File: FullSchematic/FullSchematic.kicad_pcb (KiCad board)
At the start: 4 copper layers, 106 parts, among them J1 USB_A, J10 LCD_Conn, J2 ATX-24, J3 Red Banana Jack, J4 Black Banana Jack, J5 2x6 Pin Header, J6 2x6 Pin Header, J7 CT3151-2, J8 CT3151-2, J9 2x6 Pin Header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

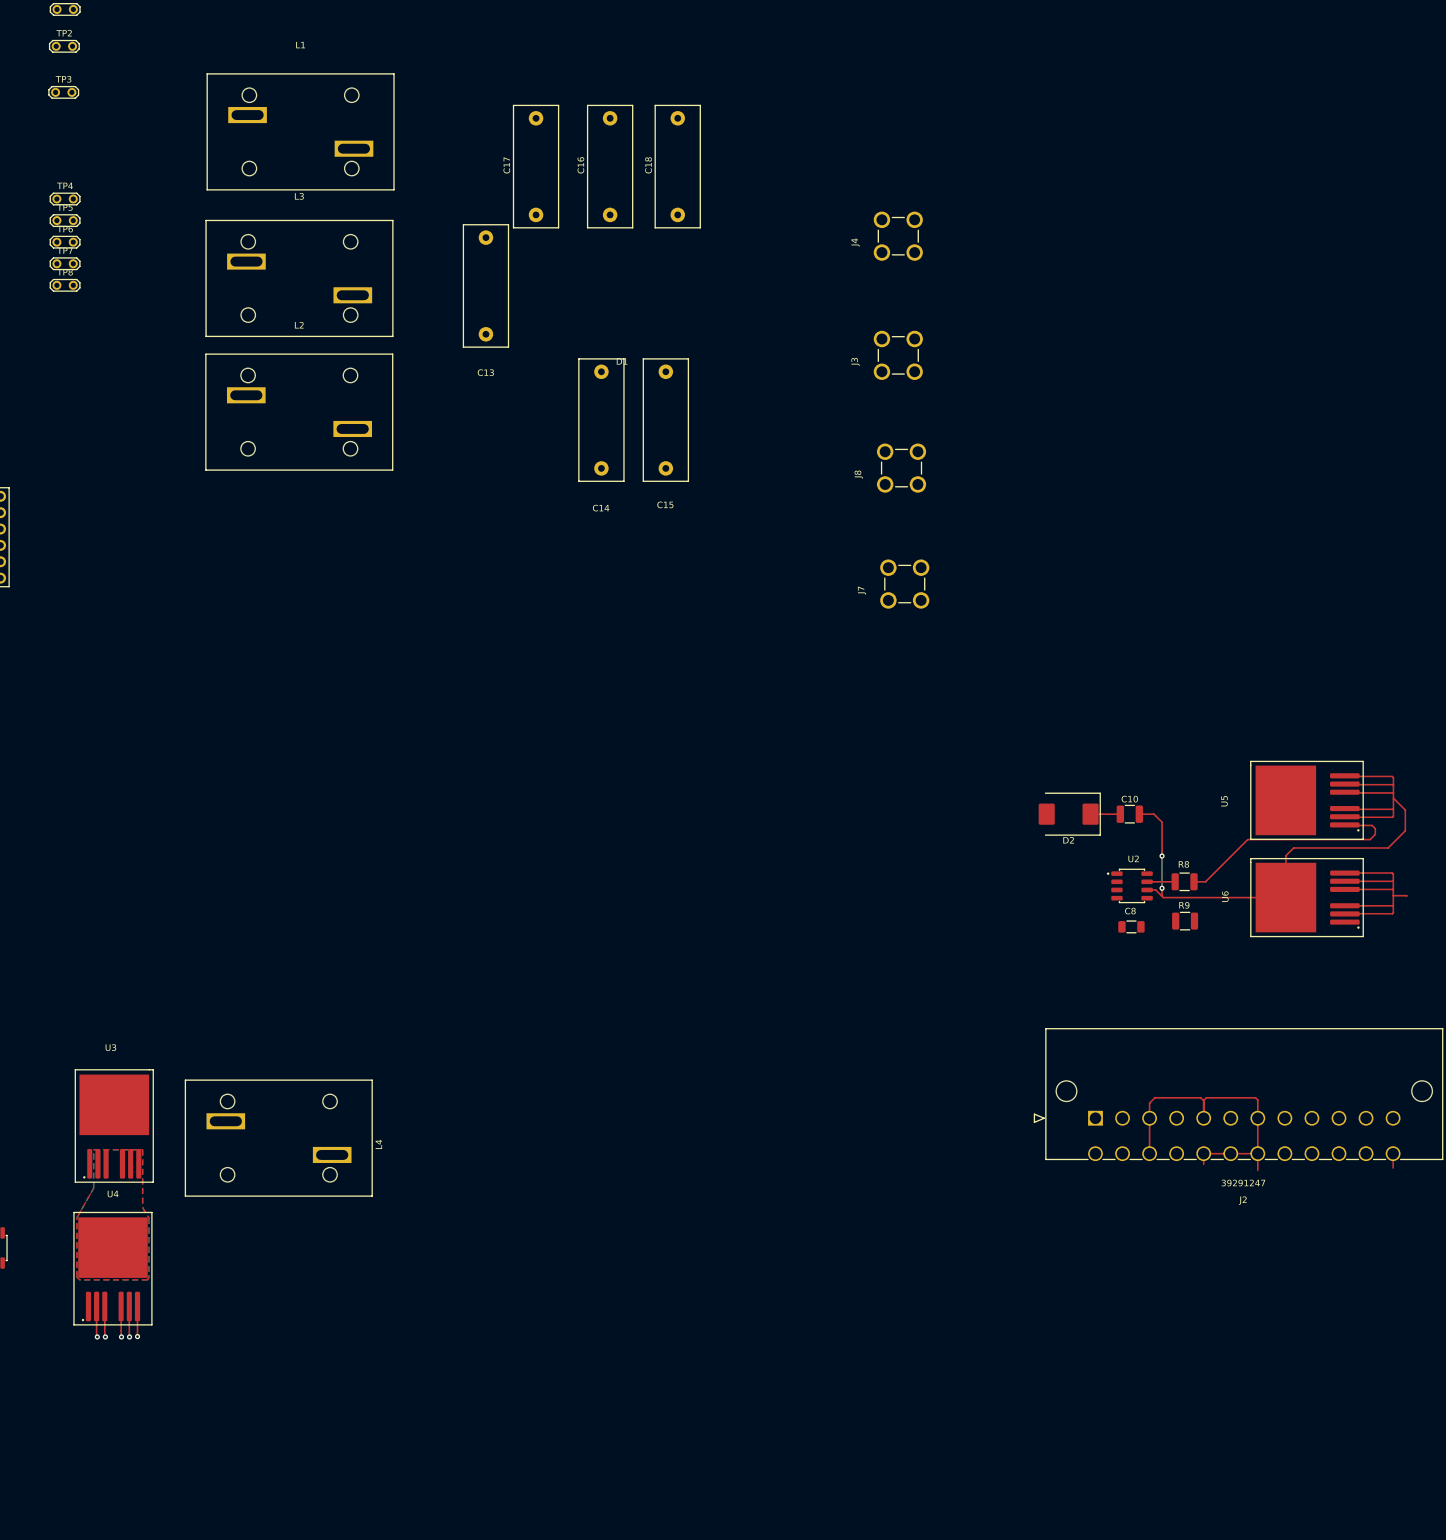
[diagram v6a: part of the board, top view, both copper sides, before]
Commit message: More Accurate Power Traces
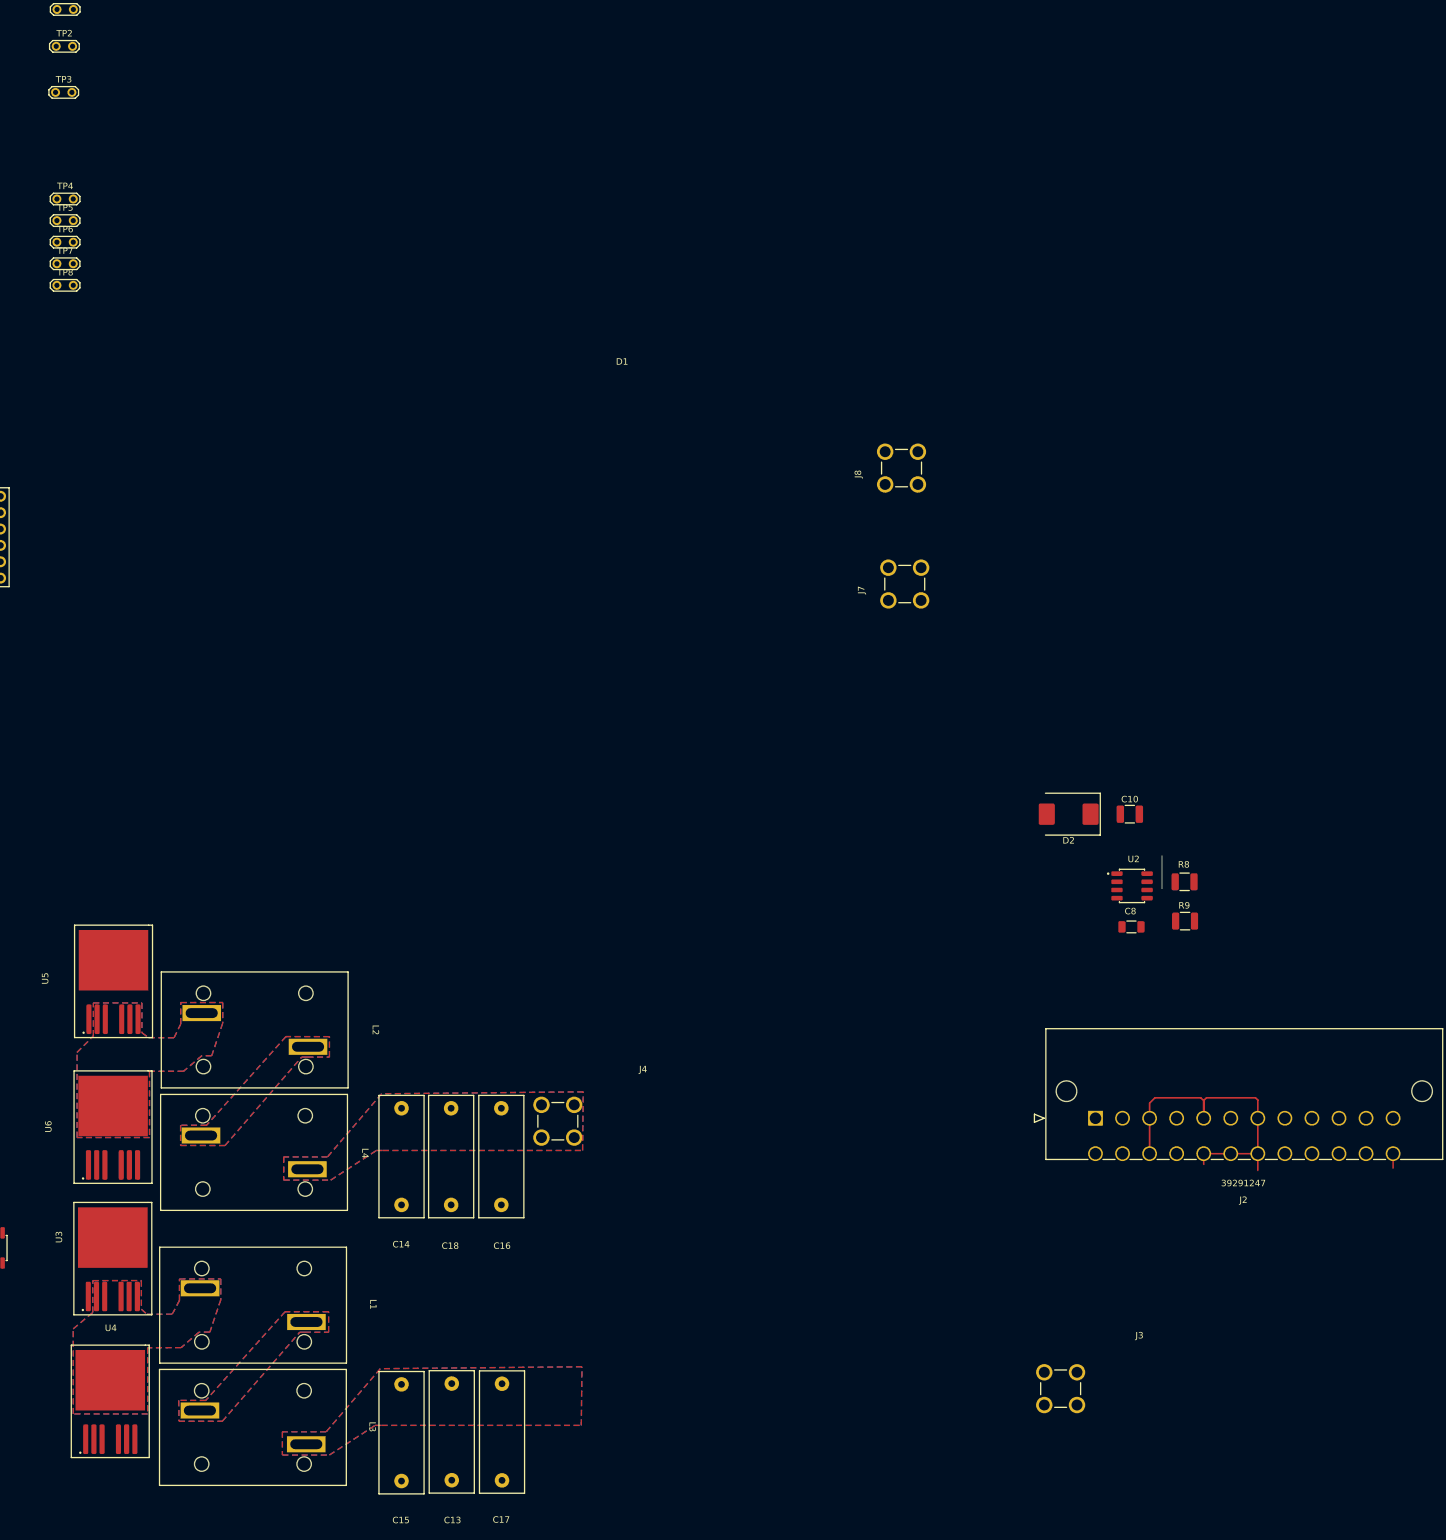
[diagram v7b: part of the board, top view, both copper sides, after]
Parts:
- moved C17 196.5 mm to (221.6, 117.6), turned to -90 degrees
- moved U6 184.9 mm to (161.2, 67.0), turned to -90 degrees
- moved U5 183.7 mm to (161.3, 44.4), turned to -90 degrees
- moved L1 182.3 mm to (182.9, 97.9)
- moved L3 178.5 mm to (182.9, 116.9)
- moved C13 178.0 mm to (213.8, 117.6), turned to -90 degrees
- moved C15 162.5 mm to (206.0, 117.7), turned to -90 degrees
- moved J3 162.4 mm to (308.3, 110.9)
- moved C18 157.6 mm to (213.7, 74.9), turned to -90 degrees
- moved C16 154.6 mm to (221.5, 74.9), turned to -90 degrees
- moved J4 147.2 mm to (230.3, 69.4)
- moved C14 118.5 mm to (206.0, 74.9), turned to -90 degrees
- moved L2 96.2 mm to (183.2, 55.2)
- moved U4 20.6 mm to (160.8, 109.6)
- moved U3 20.6 mm to (161.2, 87.4)
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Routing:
- net Net-(U2-VS): track 122.0 -> 5.00 mm, vias 2 -> 0
- net COM: track 109.2 -> 54.2 mm, vias 2 -> 0
- net Net-(U5-Gate): track 37.0 -> 0.00 mm
- net Net-(U1-VS): track 32.7 -> 18.7 mm, vias 3 -> 0
- net Net-(D2-K): track 4.62 -> 0.00 mm
- net Net-(U2-HO): track 4.36 -> 0.00 mm
- added copper zone on B.Cu, net AMP_OUT
- added copper zone on F.Cu, net AMP_OUT
- added copper zone on In1.Cu, net AMP_OUT
- added copper zone on In2.Cu, net AMP_OUT
- added copper zone on B.Cu, net Net-(L1-Pad2)
- added copper zone on F.Cu, net Net-(L1-Pad2)
- added copper zone on In1.Cu, net Net-(L1-Pad2)
- added copper zone on In2.Cu, net Net-(L1-Pad2)
- added copper zone on B.Cu, net Net-(L2-Pad2)
- added copper zone on F.Cu, net Net-(L2-Pad2)
- added copper zone on In1.Cu, net Net-(L2-Pad2)
- added copper zone on In2.Cu, net Net-(L2-Pad2)
- added copper zone on B.Cu, net Net-(U2-VS)
- added copper zone on F.Cu, net Net-(U2-VS)
- added copper zone on In1.Cu, net Net-(U2-VS)
- added copper zone on In2.Cu, net Net-(U2-VS)
- added copper zone on B.Cu, net OCTA_IN
- added copper zone on F.Cu, net OCTA_IN
- added copper zone on In1.Cu, net OCTA_IN
- added copper zone on In2.Cu, net OCTA_IN

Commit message: Added driver ICs and signal traces
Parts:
- moved TP1 263.3 mm to (98.1, 154.5)
- moved TP2 263.3 mm to (98.0, 160.2)
- moved TP3 263.3 mm to (97.9, 167.3)
- moved TP4 254.7 mm to (121.8, 179.1)
- moved TP5 254.7 mm to (121.8, 182.4)
- moved TP6 254.7 mm to (121.8, 185.8)
- moved TP7 254.7 mm to (121.8, 189.1)
- moved TP8 254.7 mm to (121.8, 192.5)
- moved C12 235.1 mm to (107.6, 165.0)
- moved R9 221.2 mm to (126.0, 129.2)
- moved C10 217.2 mm to (118.0, 104.0), turned to -90 degrees
- moved U2 214.2 mm to (120.9, 113.3), turned to 90 degrees
- moved R8 213.5 mm to (127.5, 106.8)
- moved C8 207.7 mm to (125.2, 113.2), turned to -90 degrees
- moved C1 207.3 mm to (51.7, 138.5)
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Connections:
- R6 pad 2: Net-(U1-VS) -> Net-(U3-Gate)
- U3 pad 1: Net-(U1-VS) -> Net-(U3-Gate)
- U3 pad TAB: Net-(U1-VS) -> +12V
- U4 pad 5: Net-(U1-VS) -> COM
- U4 pad 6: Net-(U1-VS) -> COM
- U4 pad 7: Net-(U1-VS) -> COM
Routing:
- net COM: track 54.2 -> 6.11 mm, vias 0 -> 4
- net Net-(U1-VS): track 18.7 -> 43.0 mm, vias 0 -> 45
- net Net-(U1-LO): track 0.15 -> 15.3 mm
- net Net-(#FLG06-pwr): track 0.00 -> 15.1 mm
- net Net-(#FLG07-pwr): track 0.00 -> 14.9 mm
- net Net-(U2-VS): track 5.00 -> 19.6 mm, vias 0 -> 29
- net Net-(U2-LO): track 0.00 -> 14.3 mm
- net +12V: track 3.35 -> 16.0 mm, vias 1 -> 88
- net Net-(U1-HO): track 0.00 -> 12.0 mm
- net Net-(U2-HO): track 0.00 -> 9.61 mm
- net Net-(U6-Gate): track 0.00 -> 5.42 mm
- net Net-(U3-Gate): track 0.00 -> 4.71 mm
- net Net-(U4-Gate): track 0.05 -> 4.15 mm
- net Net-(U5-Gate): track 0.00 -> 3.95 mm
- added copper zone on In1.Cu, net COM
- added copper zone on B.Cu, net OCTA_OUT
- added copper zone on F.Cu, net OCTA_OUT
- removed copper zone on In1.Cu, net AMP_OUT
- removed copper zone on In2.Cu, net AMP_OUT
- removed copper zone on In1.Cu, net Net-(L1-Pad2)
- removed copper zone on In2.Cu, net Net-(L1-Pad2)
- removed copper zone on In1.Cu, net Net-(L2-Pad2)
- removed copper zone on In2.Cu, net Net-(L2-Pad2)
- removed copper zone on In1.Cu, net Net-(U1-VS)
- removed copper zone on In2.Cu, net Net-(U1-VS)
- removed copper zone on In1.Cu, net Net-(U2-VS)
- removed copper zone on In2.Cu, net Net-(U2-VS)
- removed copper zone on In1.Cu, net OCTA_IN
- removed copper zone on In2.Cu, net OCTA_IN
